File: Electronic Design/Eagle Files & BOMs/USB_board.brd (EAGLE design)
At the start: 35 x 55 mm, 3 parts

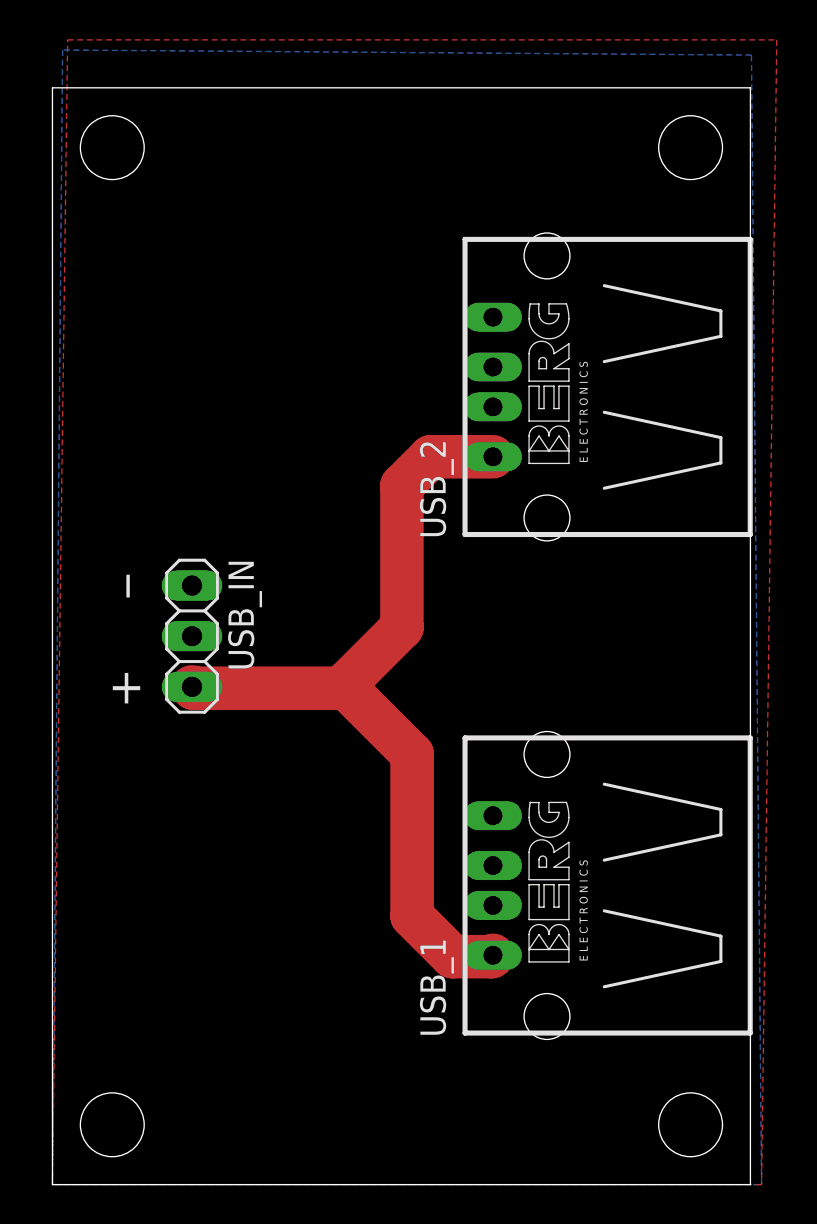
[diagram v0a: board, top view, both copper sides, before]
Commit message: reducing size of USB board
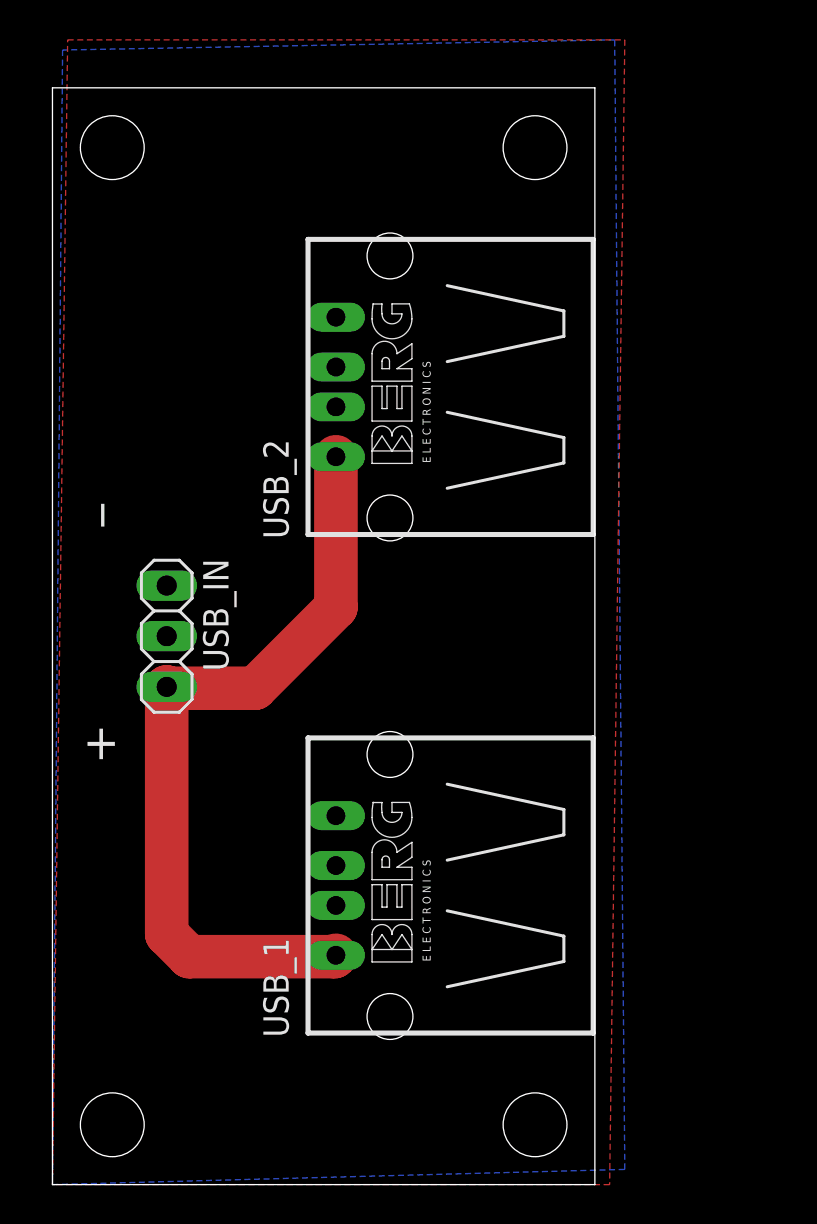
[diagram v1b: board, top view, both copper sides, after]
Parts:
- moved USB_1 7.87 mm to (16.9, 15.0)
- moved USB_2 7.87 mm to (16.9, 40.0)
- moved USB_IN 1.27 mm to (5.73, 27.5)
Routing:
- net N$1: track 42.0 -> 39.1 mm
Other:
- board size 35 x 55 mm -> 27.2 x 55 mm
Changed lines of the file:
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@@
 <board>
 <plain>
-<wire x1="0" y1="0" x2="35" y2="0" width="0" layer="20"/>
-<wire x1="35" y1="0" x2="35" y2="55" width="0" layer="20"/>
-<wire x1="35" y1="55" x2="0" y2="55" width="0" layer="20"/>
+<wire x1="0" y1="0" x2="27.2" y2="0" width="0" layer="20"/>
+<wire x1="27.2" y1="0" x2="27.2" y2="55" width="0" layer="20"/>
+<wire x1="27.2" y1="55" x2="0" y2="55" width="0" layer="20"/>
 <wire x1="0" y1="55" x2="0" y2="0" width="0" layer="20"/>
 <hole x="3" y="52" drill="3.2"/>
-<hole x="32" y="52" drill="3.2"/>
+<hole x="24.2" y="52" drill="3.2"/>
 <hole x="3" y="3" drill="3.2"/>
-<hole x="32" y="3" drill="3.2"/>
-<text x="2.794" y="24.13" size="1.778" layer="25">+</text>
-<text x="3.302" y="29.464" size="1.778" layer="25" rot="R90">_</text>
+<hole x="24.2" y="3" drill="3.2"/>
+<text x="1.524" y="21.336" size="1.778" layer="25">+</text>
+<text x="2.032" y="33.02" size="1.778" layer="25" rot="R90">_</text>
 </plain>
 <attributes>
@@
 </autorouter>
 <elements>
-<element name="USB_1" library="con-berg" package="PN87520" value="" x="24.8" y="15" rot="R90">
-<attribute name="OC_FARNELL" value="unknown" x="24.8" y="15" size="1.778" layer="27" rot="R90" display="off"/>
-<attribute name="MF" value="" x="24.8" y="15" size="1.778" layer="27" rot="R90" display="off"/>
-<attribute name="MPN" value="" x="24.8" y="15" size="1.778" layer="27" rot="R90" display="off"/>
-<attribute name="OC_NEWARK" value="unknown" x="24.8" y="15" size="1.778" layer="27" rot="R90" display="off"/>
+<element name="USB_1" library="con-berg" package="PN87520" value="" x="16.926" y="15" rot="R90">
+<attribute name="OC_FARNELL" value="unknown" x="16.926" y="15" size="1.778" layer="27" rot="R90" display="off"/>
+<attribute name="MF" value="" x="16.926" y="15" size="1.778" layer="27" rot="R90" display="off"/>
+<attribute name="MPN" value="" x="16.926" y="15" size="1.778" layer="27" rot="R90" display="off"/>
+<attribute name="OC_NEWARK" value="unknown" x="16.926" y="15" size="1.778" layer="27" rot="R90" display="off"/>
 </element>
-<element name="USB_2" library="con-berg" package="PN87520" value="" x="24.8" y="40" rot="R90">
-<attribute name="OC_FARNELL" value="unknown" x="24.8" y="40" size="1.778" layer="27" rot="R90" display="off"/>
-<attribute name="MF" value="" x="24.8" y="40" size="1.778" layer="27" rot="R90" display="off"/>
-<attribute name="MPN" value="" x="24.8" y="40" size="1.778" layer="27" rot="R90" display="off"/>
-<attribute name="OC_NEWARK" value="unknown" x="24.8" y="40" size="1.778" layer="27" rot="R90" display="off"/>
+<element name="USB_2" library="con-berg" package="PN87520" value="" x="16.926" y="40" rot="R90">
+<attribute name="OC_FARNELL" value="unknown" x="16.926" y="40" size="1.778" layer="27" rot="R90" display="off"/>
+<attribute name="MF" value="" x="16.926" y="40" size="1.778" layer="27" rot="R90" display="off"/>
+<attribute name="MPN" value="" x="16.926" y="40" size="1.778" layer="27" rot="R90" display="off"/>
+<attribute name="OC_NEWARK" value="unknown" x="16.926" y="40" size="1.778" layer="27" rot="R90" display="off"/>
 </element>
-<element name="USB_IN" library="pinhead" package="1X03" value="" x="7" y="27.5" rot="R270"/>
+<element name="USB_IN" library="pinhead" package="1X03" value="" x="5.73" y="27.5" rot="R270"/>
 </elements>
 <signals>
@@
 <contactref element="USB_1" pad="1"/>
 <contactref element="USB_2" pad="1"/>
-<wire x1="7.068" y1="24.892" x2="14.732" y2="24.892" width="2.1844" layer="1"/>
-<wire x1="7.068" y1="24.892" x2="7" y2="24.96" width="2.1844" layer="1"/>
-<wire x1="14.732" y1="24.892" x2="18.034" y2="21.59" width="2.1844" layer="1"/>
-<wire x1="18.034" y1="21.59" x2="18.034" y2="13.462" width="2.1844" layer="1"/>
-<wire x1="18.034" y1="13.462" x2="20.066" y2="11.43" width="2.1844" layer="1"/>
-<wire x1="20.066" y1="11.43" x2="22.02" y2="11.43" width="2.1844" layer="1"/>
-<wire x1="22.02" y1="11.43" x2="22.09" y2="11.5" width="2.1844" layer="1"/>
-<wire x1="14.732" y1="24.892" x2="14.732" y2="25.146" width="2.1844" layer="1"/>
-<wire x1="14.732" y1="25.146" x2="17.526" y2="27.94" width="2.1844" layer="1"/>
-<wire x1="17.526" y1="35.052" x2="17.526" y2="27.94" width="2.1844" layer="1"/>
-<wire x1="22.09" y1="36.5" x2="18.974" y2="36.5" width="2.1844" layer="1"/>
-<wire x1="18.974" y1="36.5" x2="17.526" y2="35.052" width="2.1844" layer="1"/>
+<wire x1="14.216" y1="36.5" x2="14.216" y2="28.948" width="2.1844" layer="1"/>
+<wire x1="14.216" y1="28.948" x2="10.16" y2="24.892" width="2.1844" layer="1"/>
+<wire x1="10.16" y1="24.892" x2="5.798" y2="24.892" width="2.1844" layer="1"/>
+<wire x1="5.798" y1="24.892" x2="5.73" y2="24.96" width="2.1844" layer="1"/>
+<wire x1="5.73" y1="24.96" x2="5.73" y2="12.558" width="2.1844" layer="1"/>
+<wire x1="5.73" y1="12.558" x2="6.858" y2="11.43" width="2.1844" layer="1"/>
+<wire x1="6.858" y1="11.43" x2="14.146" y2="11.43" width="2.1844" layer="1"/>
+<wire x1="14.146" y1="11.43" x2="14.216" y2="11.5" width="2.1844" layer="1"/>
 </signal>
 <signal name="GND">
 <polygon width="2.54" layer="1">
 <vertex x="0.762" y="57.404"/>
-<vertex x="36.322" y="57.404"/>
-<vertex x="35.56" y="0"/>
+<vertex x="28.702" y="57.404"/>
+<vertex x="27.94" y="0"/>
 <vertex x="0" y="0"/>
 </polygon>
@@
 <vertex x="0.508" y="56.896"/>
 <vertex x="0" y="0"/>
-<vertex x="35.56" y="0"/>
-<vertex x="35.052" y="56.642"/>
+<vertex x="28.702" y="0.762"/>
+<vertex x="28.194" y="57.404"/>
 </polygon>
 </signal>

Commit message: made PCB smaller
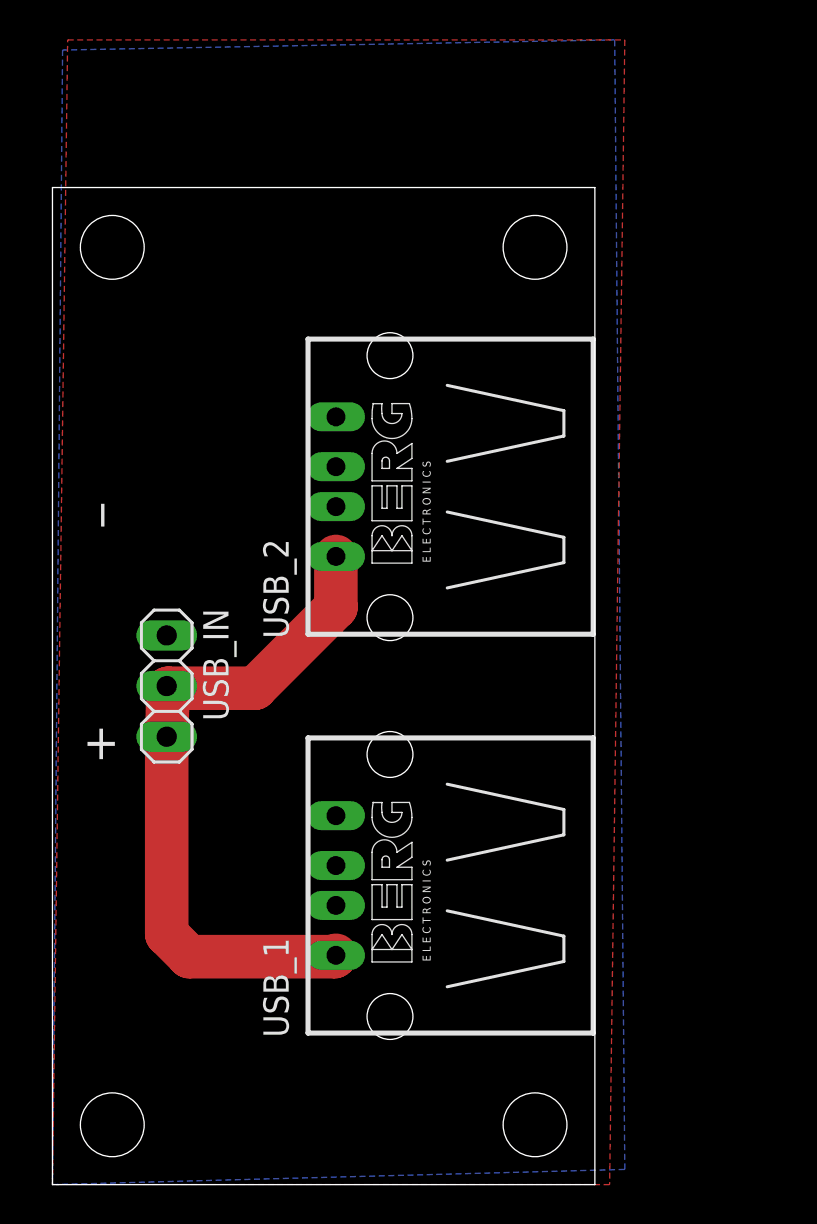
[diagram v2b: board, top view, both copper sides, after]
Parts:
- moved USB_2 5.00 mm to (16.9, 35.0)
- moved USB_IN 2.50 mm to (5.73, 25.0)
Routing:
- net N$1: track 39.1 -> 34.0 mm
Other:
- board size 27.2 x 55 mm -> 27.2 x 50 mm
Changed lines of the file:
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@@
 <plain>
 <wire x1="0" y1="0" x2="27.2" y2="0" width="0" layer="20"/>
-<wire x1="27.2" y1="0" x2="27.2" y2="55" width="0" layer="20"/>
-<wire x1="27.2" y1="55" x2="0" y2="55" width="0" layer="20"/>
-<wire x1="0" y1="55" x2="0" y2="0" width="0" layer="20"/>
-<hole x="3" y="52" drill="3.2"/>
-<hole x="24.2" y="52" drill="3.2"/>
+<wire x1="27.2" y1="0" x2="27.2" y2="50" width="0" layer="20"/>
+<wire x1="27.2" y1="50" x2="0" y2="50" width="0" layer="20"/>
+<wire x1="0" y1="50" x2="0" y2="0" width="0" layer="20"/>
+<hole x="3" y="47" drill="3.2"/>
+<hole x="24.2" y="47" drill="3.2"/>
 <hole x="3" y="3" drill="3.2"/>
 <hole x="24.2" y="3" drill="3.2"/>
@@
 <attribute name="OC_NEWARK" value="unknown" x="16.926" y="15" size="1.778" layer="27" rot="R90" display="off"/>
 </element>
-<element name="USB_2" library="con-berg" package="PN87520" value="" x="16.926" y="40" rot="R90">
-<attribute name="OC_FARNELL" value="unknown" x="16.926" y="40" size="1.778" layer="27" rot="R90" display="off"/>
-<attribute name="MF" value="" x="16.926" y="40" size="1.778" layer="27" rot="R90" display="off"/>
-<attribute name="MPN" value="" x="16.926" y="40" size="1.778" layer="27" rot="R90" display="off"/>
-<attribute name="OC_NEWARK" value="unknown" x="16.926" y="40" size="1.778" layer="27" rot="R90" display="off"/>
+<element name="USB_2" library="con-berg" package="PN87520" value="" x="16.926" y="35" rot="R90">
+<attribute name="OC_FARNELL" value="unknown" x="16.926" y="35" size="1.778" layer="27" rot="R90" display="off"/>
+<attribute name="MF" value="" x="16.926" y="35" size="1.778" layer="27" rot="R90" display="off"/>
+<attribute name="MPN" value="" x="16.926" y="35" size="1.778" layer="27" rot="R90" display="off"/>
+<attribute name="OC_NEWARK" value="unknown" x="16.926" y="35" size="1.778" layer="27" rot="R90" display="off"/>
 </element>
-<element name="USB_IN" library="pinhead" package="1X03" value="" x="5.73" y="27.5" rot="R270"/>
+<element name="USB_IN" library="pinhead" package="1X03" value="" x="5.73" y="25" rot="R270"/>
 </elements>
 <signals>
@@
 <contactref element="USB_1" pad="1"/>
 <contactref element="USB_2" pad="1"/>
-<wire x1="14.216" y1="36.5" x2="14.216" y2="28.948" width="2.1844" layer="1"/>
+<wire x1="14.216" y1="31.5" x2="14.216" y2="28.948" width="2.1844" layer="1"/>
 <wire x1="14.216" y1="28.948" x2="10.16" y2="24.892" width="2.1844" layer="1"/>
 <wire x1="10.16" y1="24.892" x2="5.798" y2="24.892" width="2.1844" layer="1"/>
-<wire x1="5.798" y1="24.892" x2="5.73" y2="24.96" width="2.1844" layer="1"/>
-<wire x1="5.73" y1="24.96" x2="5.73" y2="12.558" width="2.1844" layer="1"/>
+<wire x1="5.798" y1="24.892" x2="5.73" y2="22.46" width="2.1844" layer="1"/>
+<wire x1="5.73" y1="22.46" x2="5.73" y2="12.558" width="2.1844" layer="1"/>
 <wire x1="5.73" y1="12.558" x2="6.858" y2="11.43" width="2.1844" layer="1"/>
 <wire x1="6.858" y1="11.43" x2="14.146" y2="11.43" width="2.1844" layer="1"/>

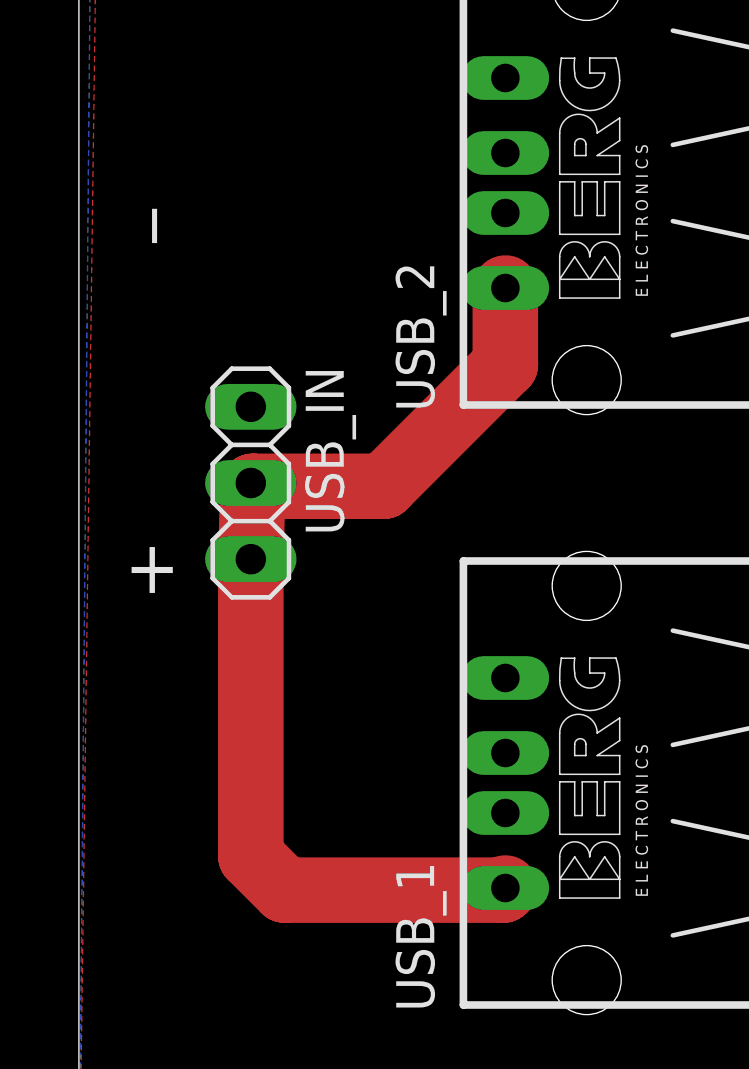
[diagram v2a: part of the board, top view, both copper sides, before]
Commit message: minor changes to USB board and updating gerbers
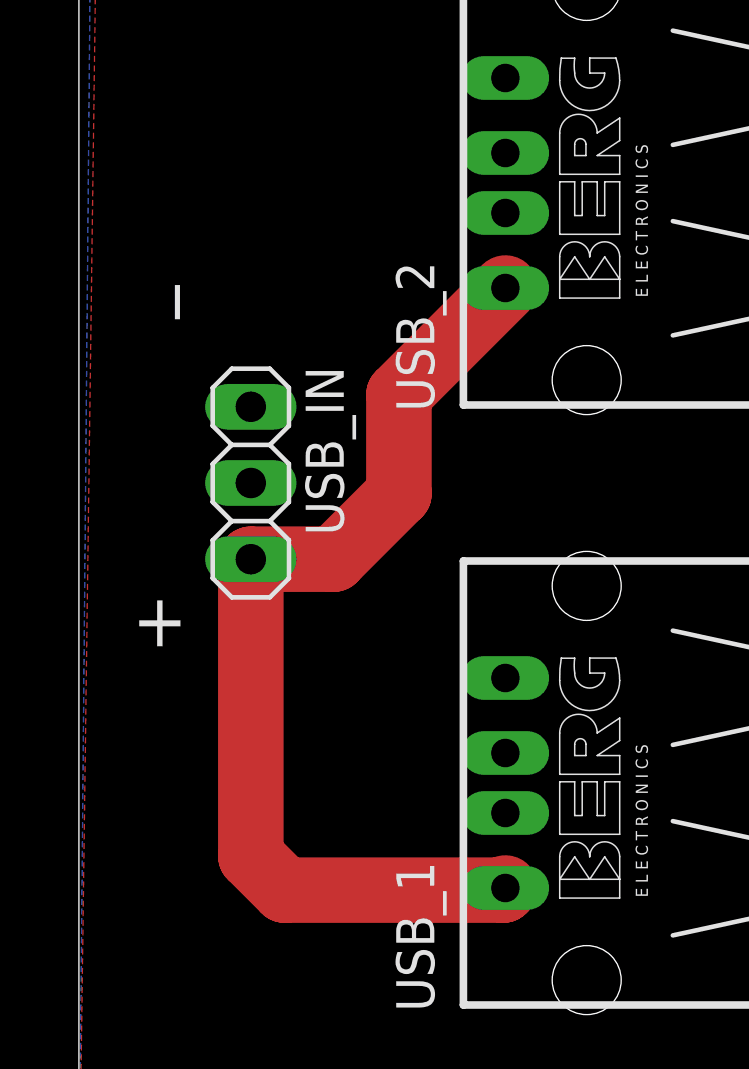
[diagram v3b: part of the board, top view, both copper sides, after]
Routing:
- net N$1: track 34.0 -> 33.1 mm
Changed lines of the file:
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@@
 <hole x="3" y="3" drill="3.2"/>
 <hole x="24.2" y="3" drill="3.2"/>
-<text x="1.524" y="21.336" size="1.778" layer="25">+</text>
-<text x="2.032" y="33.02" size="1.778" layer="25" rot="R90">_</text>
+<text x="1.778" y="19.558" size="1.778" layer="25">+</text>
+<text x="2.794" y="30.48" size="1.778" layer="25" rot="R90">_</text>
 </plain>
 <attributes>
@@
 </class>
 </classes>
-<designrules name="default">
+<designrules name="default *">
 <description language="de">&lt;b&gt;EAGLE Design Rules&lt;/b&gt;
 &lt;p&gt;
@@
 <param name="mdSmdStop" value="0mil"/>
 <param name="msWidth" value="10mil"/>
-<param name="msDrill" value="24mil"/>
+<param name="msDrill" value="20mil"/>
 <param name="msMicroVia" value="9.99mm"/>
 <param name="msBlindViaRatio" value="0.5"/>
@@
 <contactref element="USB_1" pad="1"/>
 <contactref element="USB_2" pad="1"/>
-<wire x1="14.216" y1="31.5" x2="14.216" y2="28.948" width="2.1844" layer="1"/>
-<wire x1="14.216" y1="28.948" x2="10.16" y2="24.892" width="2.1844" layer="1"/>
-<wire x1="10.16" y1="24.892" x2="5.798" y2="24.892" width="2.1844" layer="1"/>
-<wire x1="5.798" y1="24.892" x2="5.73" y2="22.46" width="2.1844" layer="1"/>
-<wire x1="5.73" y1="22.46" x2="5.73" y2="12.558" width="2.1844" layer="1"/>
+<wire x1="5.73" y1="12.558" x2="5.73" y2="22.46" width="2.1844" layer="1"/>
 <wire x1="5.73" y1="12.558" x2="6.858" y2="11.43" width="2.1844" layer="1"/>
 <wire x1="6.858" y1="11.43" x2="14.146" y2="11.43" width="2.1844" layer="1"/>
 <wire x1="14.146" y1="11.43" x2="14.216" y2="11.5" width="2.1844" layer="1"/>
+<wire x1="5.73" y1="22.46" x2="8.49" y2="22.46" width="2.1844" layer="1"/>
+<wire x1="8.49" y1="22.46" x2="10.668" y2="24.638" width="2.1844" layer="1"/>
+<wire x1="10.668" y1="24.638" x2="10.668" y2="27.952" width="2.1844" layer="1"/>
+<wire x1="10.668" y1="27.952" x2="14.216" y2="31.5" width="2.1844" layer="1"/>
 </signal>
 <signal name="GND">
